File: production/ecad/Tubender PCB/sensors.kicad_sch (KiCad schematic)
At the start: 0 parts

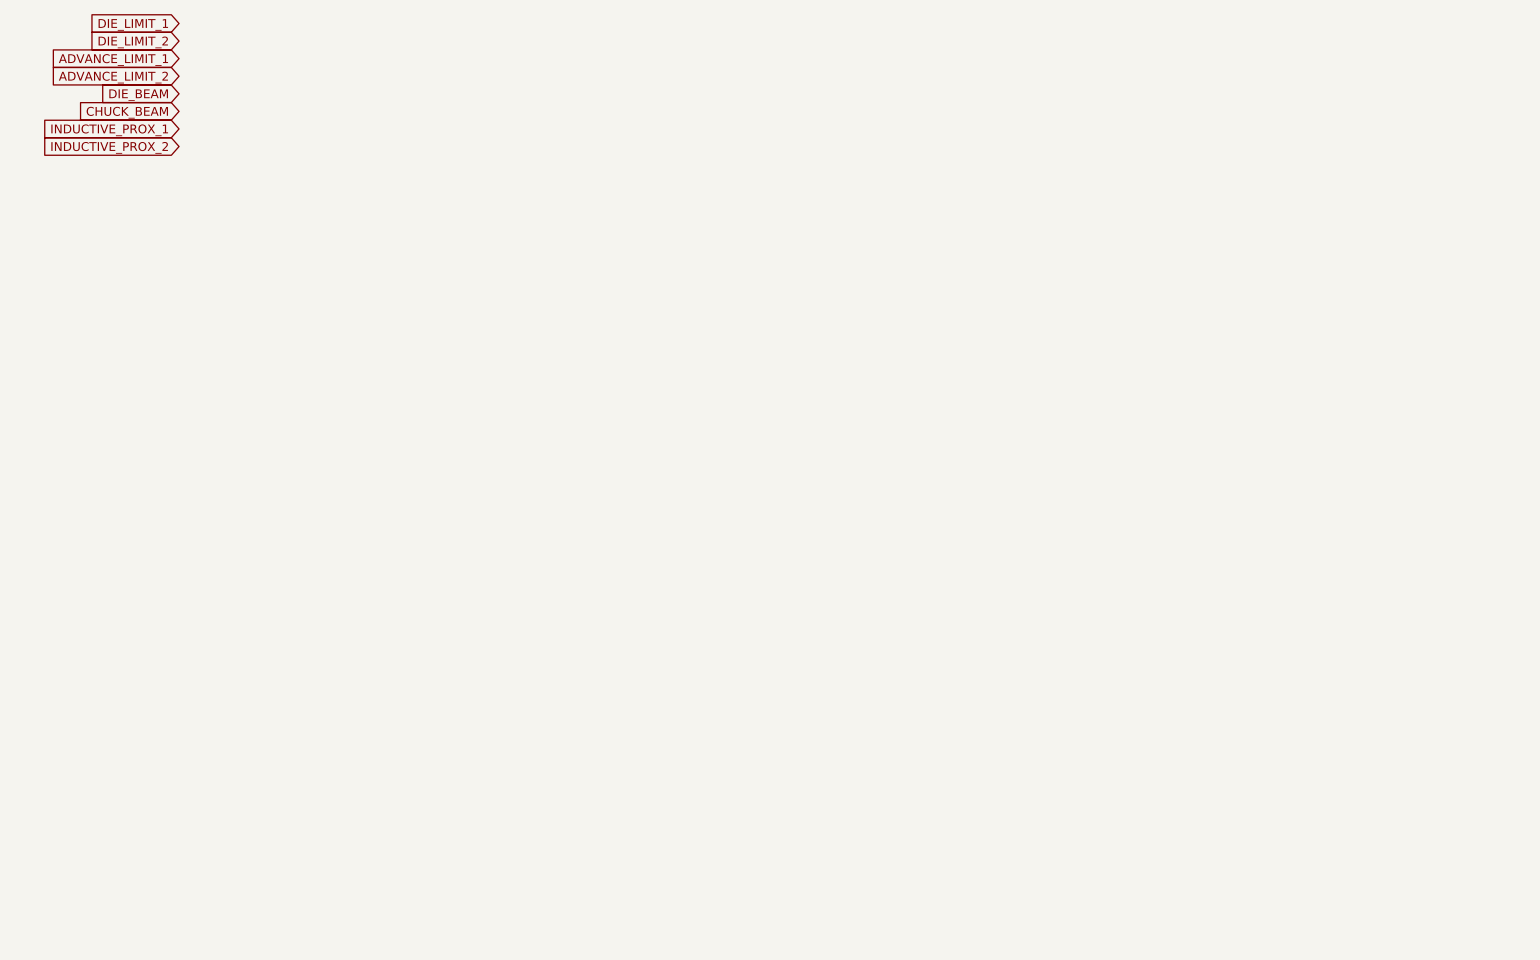
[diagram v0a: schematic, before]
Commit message: sensor connectors - niki
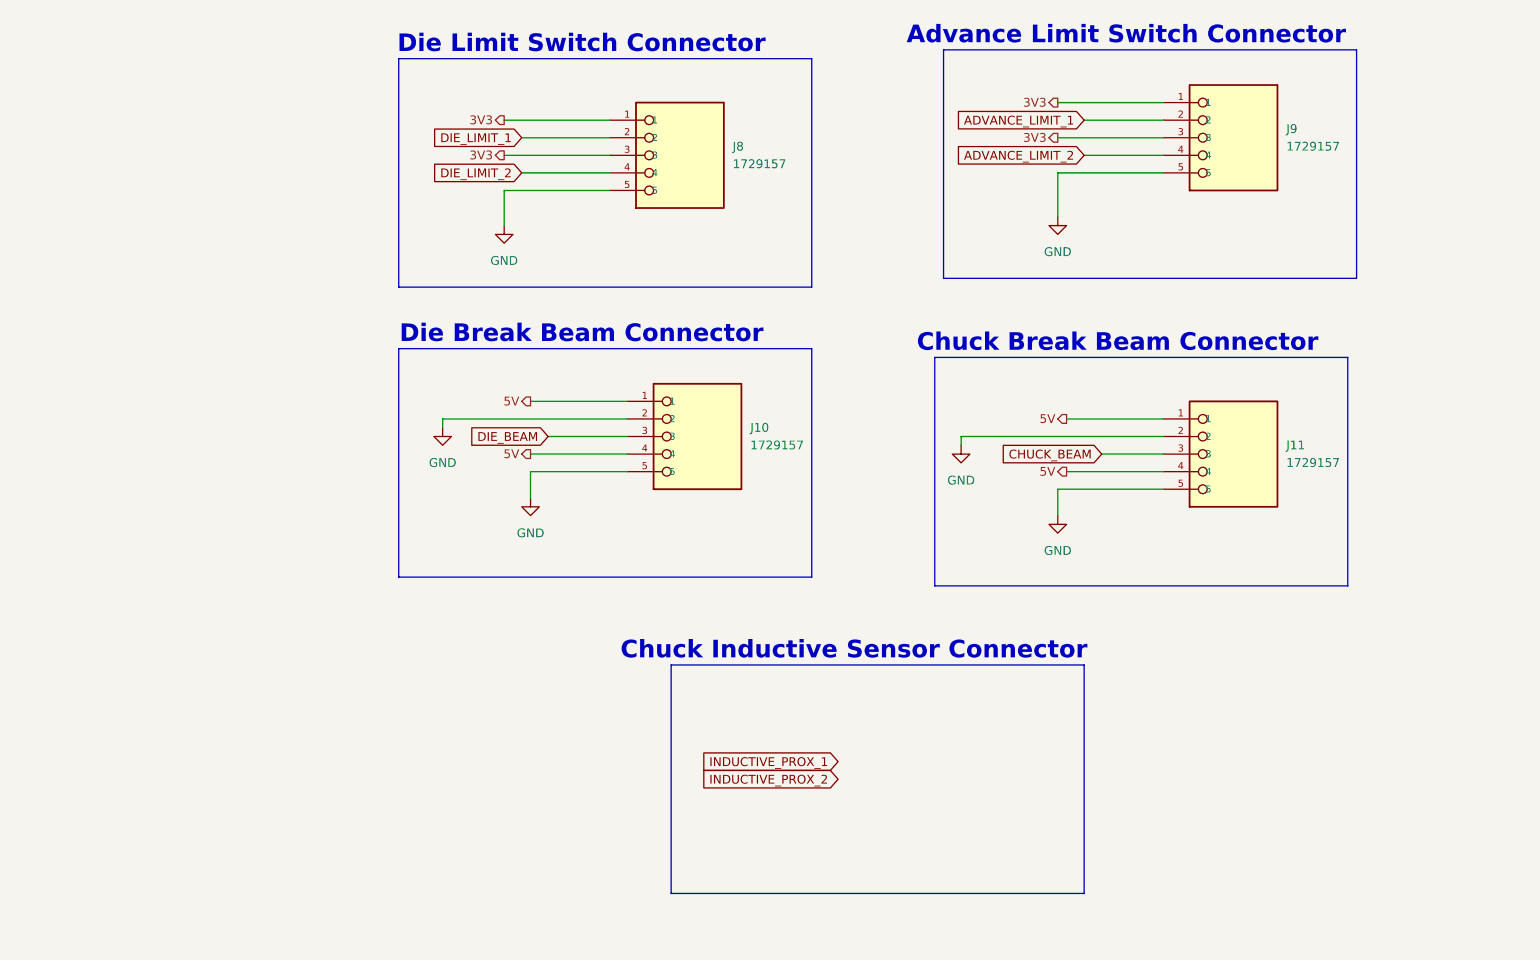
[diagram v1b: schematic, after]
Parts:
- added J10, J11, J8, J9: 1729157, 1729157:PHOENIX_1729157, symbol 1729157:1729157
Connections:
- net ADVANCE_LIMIT_1: now also J9.2
- net ADVANCE_LIMIT_2: now also J9.4
- net CHUCK_BEAM: now also J11.3
- net DIE_BEAM: now also J10.3
- net DIE_LIMIT_1: now also J8.2
- net DIE_LIMIT_2: now also J8.4
- new net 3V3: J8.1, J8.3, J9.1, J9.3
- new net 5V: J10.1, J10.4, J11.1, J11.4
- new net GND: J10.2, J10.5, J11.2, J11.5, J8.5, J9.5
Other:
- note added: "Advance Limit Switch Connector"
- note added: "Chuck Break Beam Connector"
- note added: "Chuck Inductive Sensor Connector"
- note added: "Die Break Beam Connector"
- note added: "Die Limit Switch Connector"

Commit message: sensors!
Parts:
- removed J8, J9: 1729157, 1729157:PHOENIX_1729157, symbol 1729157:1729157
- added J12, J8, J9: 1729160, CONN_1729160_PXC, symbol 1729160:1729160
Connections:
- net ADVANCE_LIMIT_1: now also J9.2
- net ADVANCE_LIMIT_2: now also J9.5
- net DIE_LIMIT_1: now also J8.2
- net DIE_LIMIT_2: now also J8.5
- net GND: now also J12.3, J12.6, J8.3, J8.6, J9.3, J9.6
- net INDUCTIVE_PROX_1: now also J12.2
- net INDUCTIVE_PROX_2: now also J12.5
- new net 12V: J12.1, J12.4, J8.1, J8.4, J9.1, J9.4
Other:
- note added: "Bending Linear Potentiometer"

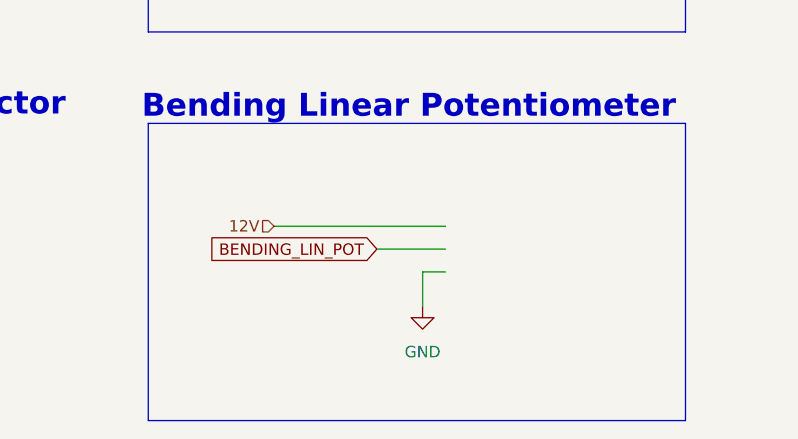
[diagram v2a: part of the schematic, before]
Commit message: adding 3pin connector
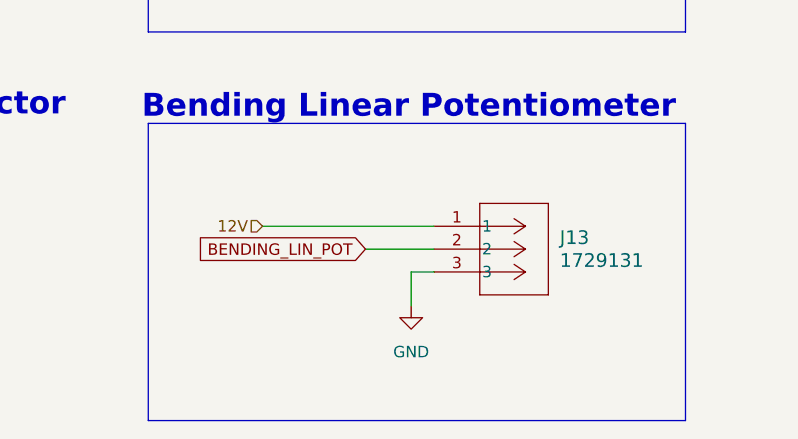
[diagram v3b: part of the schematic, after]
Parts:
- added J13: 1729131, CONN_1729131_PXC, symbol 1729131:1729131
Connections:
- net 12V: now also J13.1
- net BENDING_LIN_POT: now also J13.2
- net GND: now also J13.3
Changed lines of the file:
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@@
 	(wire
 		(pts
-			(xy 170.18 128.27) (xy 177.8 128.27)
+			(xy 168.91 128.27) (xy 176.53 128.27)
 		)
 		(stroke
@@
 	(wire
 		(pts
-			(xy 177.8 130.81) (xy 175.26 130.81)
+			(xy 176.53 130.81) (xy 173.99 130.81)
 		)
 		(stroke
@@
 	(wire
 		(pts
-			(xy 175.26 130.81) (xy 175.26 134.62)
+			(xy 173.99 130.81) (xy 173.99 134.62)
 		)
 		(stroke
@@
 	(wire
 		(pts
-			(xy 158.75 125.73) (xy 177.8 125.73)
+			(xy 157.48 125.73) (xy 176.53 125.73)
 		)
 		(stroke
@@
 	(global_label "BENDING_LIN_POT"
 		(shape input)
-		(at 170.18 128.27 180)
+		(at 168.91 128.27 180)
 		(fields_autoplaced yes)
 		(effects
@@
 		)
 		(property "Intersheetrefs" "${INTERSHEET_REFS}"
-			(at 150.5033 128.27 0)
+			(at 149.2333 128.27 0)
 			(effects
 				(font
@@
 	(hierarchical_label "12V"
 		(shape input)
-		(at 158.75 125.73 180)
+		(at 157.48 125.73 180)
 		(fields_autoplaced yes)
 		(effects
@@
 	)
 	(symbol
+		(lib_id "1729131:1729131")
+		(at 176.53 125.73 0)
+		(unit 1)
+		(exclude_from_sim no)
+		(in_bom yes)
+		(on_board yes)
+		(dnp no)
+		(fields_autoplaced yes)
+		(property "Reference" "J13"
+			(at 190.5 126.9999 0)
+			(effects
+				(font
+					(size 1.524 1.524)
+				)
+				(justify left)
+			)
+		)
+		(property "Value" "1729131"
+			(at 190.5 129.5399 0)
+			(effects
+				(font
+					(size 1.524 1.524)
+				)
+				(justify left)
+			)
+		)
+		(property "Footprint" "CONN_1729131_PXC"
+			(at 176.53 125.73 0)
+			(effects
+				(font
+					(size 1.27 1.27)
+					(italic yes)
+				)
+				(hide yes)
+			)
+		)
+		(property "Datasheet" "1729131"
+			(at 176.53 125.73 0)
+			(effects
+				(font
+					(size 1.27 1.27)
+					(italic yes)
+				)
+				(hide yes)
+			)
+		)
+		(property "Description" ""
+			(at 176.53 125.73 0)
+			(effects
+				(font
+					(size 1.27 1.27)
+				)
+				(hide yes)
+			)
+		)
+		(pin "1"
+		)
+		(pin "2"
+		)
+		(pin "3"
+		)
+		(instances
+			(project ""
+				(path "/3e1aedd0-6089-4edb-92c7-0c31da2e7927/cace885d-07c2-48b7-a983-3b69a09d8a62"
+					(reference "J13")
+					(unit 1)
+				)
+			)
+		)
+	)
+	(symbol
 		(lib_id "1729160:1729160")
 		(at 177.8 35.56 0)
@@
 	(symbol
 		(lib_id "power:GND")
-		(at 175.26 134.62 0)
+		(at 173.99 134.62 0)
 		(unit 1)
 		(exclude_from_sim no)
@@
 		(fields_autoplaced yes)
 		(property "Reference" "#PWR042"
-			(at 175.26 140.97 0)
+			(at 173.99 140.97 0)
 			(effects
 				(font
@@
 		)
 		(property "Value" "GND"
-			(at 175.26 139.7 0)
+			(at 173.99 139.7 0)
 			(effects
 				(font
@@
 		)
 		(property "Footprint" ""
-			(at 175.26 134.62 0)
+			(at 173.99 134.62 0)
 			(effects
 				(font
@@
 		)
 		(property "Datasheet" ""
-			(at 175.26 134.62 0)
+			(at 173.99 134.62 0)
 			(effects
 				(font
@@
 		)
 		(property "Description" "Power symbol creates a global label with name \"GND\" , ground"
-			(at 175.26 134.62 0)
-			(effects
-				(font
+			(at 173.99 134.62 0)
+			(effects
+				(font

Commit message: Formatting
Boom
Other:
- moved on the sheet: J10, J11, J12, J13, J8, J9

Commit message: final for rev 1
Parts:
- removed J10, J11: 1729157, 1729157:PHOENIX_1729157, symbol 1729157:1729157
- removed J12, J8, J9: 1729160, CONN_1729160_PXC, symbol 1729160:1729160
- removed J13: 1729131, CONN_1729131_PXC, symbol 1729131:1729131
- added J10, J9: 640445-5, 640445-5:TE_640445-5, symbol 640445-5:640445-5
- added J11, J5, J8: 640445-6, 640445-6:TE_640445-6, symbol 640445-6:640445-6
- added J12: B3P-VH, CONN3X1_B3P-VH_JST, symbol 2024-10-11_08-07-43:B3P-VH
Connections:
- net 12V: now also J11.1, J11.4, J5.1, J5.4, J8.1, J8.4
- net 5V: now also J10.1, J10.4, J9.1, J9.4
- net ADVANCE_LIMIT_1: now also J8.2
- net ADVANCE_LIMIT_2: now also J8.5
- net BENDING_LIN_POT: now also J12.2
- net CHUCK_BEAM: now also J10.3
- net DIE_BEAM: now also J9.3
- net DIE_LIMIT_1: now also J5.2
- net DIE_LIMIT_2: now also J5.5
- net GND: now also J10.2, J10.5, J11.3, J11.6, J12.3, J5.3, J5.6, J8.3, J8.6, J9.2, J9.5
- net INDUCTIVE_PROX_1: now also J11.2
- net INDUCTIVE_PROX_2: now also J11.5
- new net 24V: J12.1

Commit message: Fixed Button Connectors
All done! Enjoy :)
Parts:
- removed J10, J9: 640445-5, 640445-5:TE_640445-5, symbol 640445-5:640445-5
- removed J11, J5, J8: 640445-6, 640445-6:TE_640445-6, symbol 640445-6:640445-6
- removed J12: B3P-VH, CONN3X1_B3P-VH_JST, symbol 2024-10-11_08-07-43:B3P-VH
- added J10, J9: 640387-5, 640387-5:TE_640387-5, symbol 640387-5:640387-5
- added J14: 640387-3, 640387-3:TE_640387-3, symbol 640387-3:640387-3
- added J5, J6, J8: 640387-6, 640387-6:TE_640387-6, symbol 640387-6:640387-6
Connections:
- net 12V: now also J5.1, J5.4, J6.1, J6.4, J8.1, J8.4
- net 24V: now also J14.1
- net 5V: now also J10.1, J10.4, J9.1, J9.4
- net ADVANCE_LIMIT_1: now also J6.2
- net ADVANCE_LIMIT_2: now also J6.5
- net BENDING_LIN_POT: now also J14.2
- net CHUCK_BEAM: now also J10.3
- net DIE_BEAM: now also J9.3
- net DIE_LIMIT_1: now also J5.2
- net DIE_LIMIT_2: now also J5.5
- net GND: now also J10.2, J10.5, J14.3, J5.3, J5.6, J6.3, J6.6, J8.3, J8.6, J9.2, J9.5
- net INDUCTIVE_PROX_1: now also J8.2
- net INDUCTIVE_PROX_2: now also J8.5
